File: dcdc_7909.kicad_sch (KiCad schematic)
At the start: 50 parts, among them J1 V_IN, J2 G_IN, J3 RFShield_OnePiece, J4 +10V, J5 G_OUT, J6 -10V, U1 LM2940-SOT223, U2 LT3471, U3 LT3045xMSE, U4 LT3094xMSE

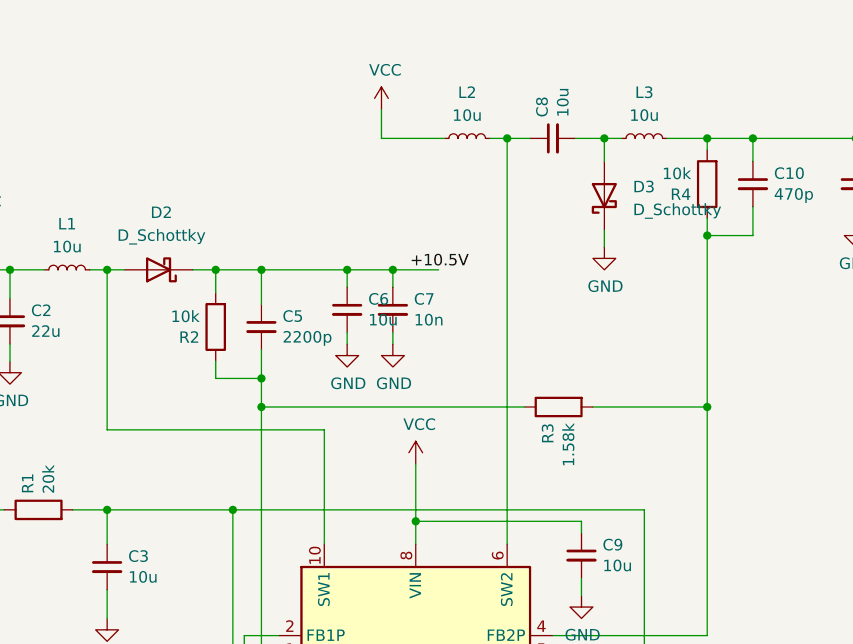
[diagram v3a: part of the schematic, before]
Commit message: Updated BOM.
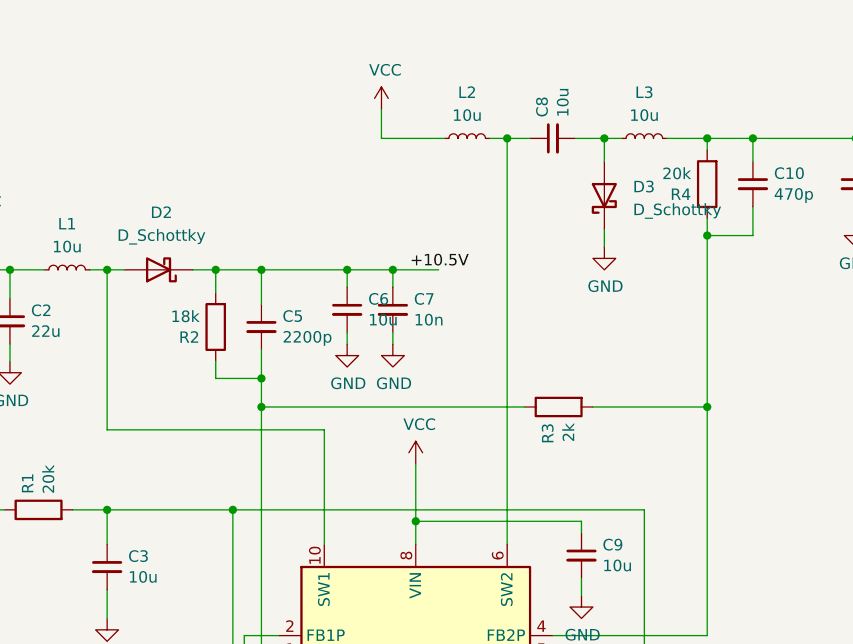
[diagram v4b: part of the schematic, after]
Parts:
- D1: LCSC (none) -> DO NOT POPULATE
- R2: value 10k -> 18k; LCSC (none) -> C25810
- R3: value 1.58k -> 2k; LCSC (none) -> C22975
- R4: value 10k -> 20k; LCSC (none) -> C4184
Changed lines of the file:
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@@
       (effects (font (size 1.27 1.27)) (justify left))
     )
-    (property "Value" "1.58k" (id 1) (at 109.728 114.173 0)
+    (property "Value" "2k" (id 1) (at 109.728 114.173 0)
       (effects (font (size 1.27 1.27)) (justify left))
     )
@@
     )
     (property "Datasheet" "~" (id 3) (at 108.585 112.395 0)
+      (effects (font (size 1.27 1.27)) hide)
+    )
+    (property "LCSC" "C22975" (id 4) (at 108.585 112.395 0)
       (effects (font (size 1.27 1.27)) hide)
     )
@@
   (symbol (lib_id "power:GND") (at 113.665 94.615 0) (unit 1)
     (in_bom yes) (on_board yes)
-    (property "Reference" "#PWR?" (id 0) (at 113.665 100.965 0)
+    (property "Reference" "#PWR0101" (id 0) (at 113.665 100.965 0)
       (effects (font (size 1.27 1.27)) hide)
     )
@@
       (effects (font (size 1.27 1.27)) (justify left))
     )
-    (property "Value" "10k" (id 1) (at 123.317 86.487 0)
+    (property "Value" "20k" (id 1) (at 123.317 86.487 0)
       (effects (font (size 1.27 1.27)) (justify left))
     )
@@
     )
     (property "Datasheet" "~" (id 3) (at 125.095 87.63 0)
+      (effects (font (size 1.27 1.27)) hide)
+    )
+    (property "LCSC" "C4184" (id 4) (at 125.095 87.63 0)
       (effects (font (size 1.27 1.27)) hide)
     )
@@
       (effects (font (size 1.27 1.27)) (justify left))
     )
-    (property "Value" "10k" (id 1) (at 68.707 102.362 0)
+    (property "Value" "18k" (id 1) (at 68.707 102.362 0)
       (effects (font (size 1.27 1.27)) (justify left))
     )
@@
     )
     (property "Datasheet" "~" (id 3) (at 70.485 103.505 0)
+      (effects (font (size 1.27 1.27)) hide)
+    )
+    (property "LCSC" "C25810" (id 4) (at 70.485 103.505 0)
       (effects (font (size 1.27 1.27)) hide)
     )
@@
       (effects (font (size 1.27 1.27)) hide)
     )
+    (property "LCSC" "DO NOT POPULATE" (id 4) (at 45.085 40.005 0)
+      (effects (font (size 1.27 1.27)) hide)
+    )
     (pin "1")
     (pin "2")
@@
     )
     (path "/238e584d-5d8d-4459-9620-7e15c60342c4"
-      (reference "#PWR?") (unit 1) (value "GND") (footprint "")
+      (reference "#PWR0101") (unit 1) (value "GND") (footprint "")
     )
     (path "/aa882a6c-bc17-4b7e-9561-d17811dd5eb5"
@@
     )
     (path "/90e51816-a1d4-45a7-942c-682d8cce5b3b"
-      (reference "R2") (unit 1) (value "10k") (footprint "Resistor_SMD:R_0603_1608Metric")
+      (reference "R2") (unit 1) (value "18k") (footprint "Resistor_SMD:R_0603_1608Metric")
     )
     (path "/18aa7285-da5c-42b6-a485-257c708a9352"
-      (reference "R3") (unit 1) (value "1.58k") (footprint "Resistor_SMD:R_0603_1608Metric")
+      (reference "R3") (unit 1) (value "2k") (footprint "Resistor_SMD:R_0603_1608Metric")
     )
     (path "/3090092e-4c9a-4661-95c3-730de5416b81"
-      (reference "R4") (unit 1) (value "10k") (footprint "Resistor_SMD:R_0603_1608Metric")
+      (reference "R4") (unit 1) (value "20k") (footprint "Resistor_SMD:R_0603_1608Metric")
     )
     (path "/00000000-0000-0000-0000-00005ea01b91"

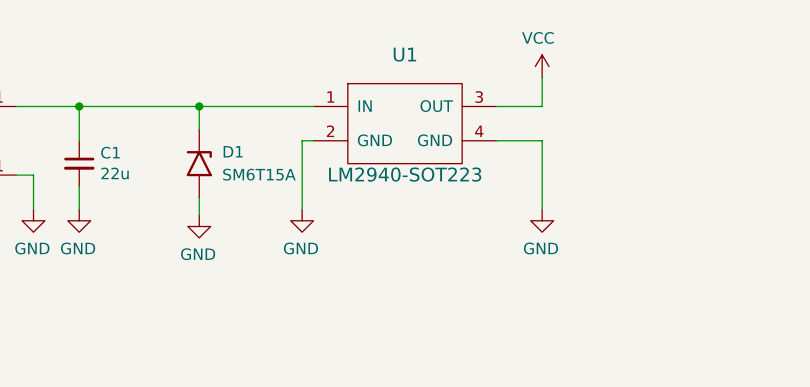
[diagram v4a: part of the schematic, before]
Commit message: Corrected the ground plane.
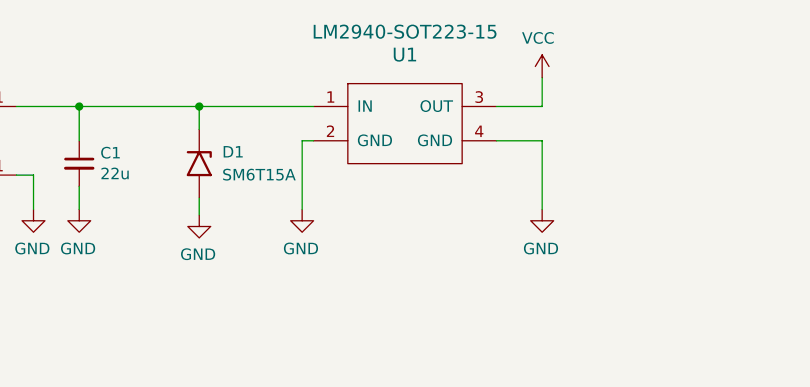
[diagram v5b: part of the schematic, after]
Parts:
- D1: LCSC DO NOT POPULATE -> C80394
- U1: value LM2940-SOT223 -> LM2940-SOT223-15
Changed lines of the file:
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@@
       (effects (font (size 1.524 1.524)))
     )
-    (property "Value" "LM2940-SOT223" (id 1) (at 67.945 41.275 0)
+    (property "Value" "LM2940-SOT223-15" (id 1) (at 67.945 25.4 0)
       (effects (font (size 1.524 1.524)))
     )
@@
       (effects (font (size 1.27 1.27)) hide)
     )
-    (property "LCSC" "DO NOT POPULATE" (id 4) (at 45.085 40.005 0)
+    (property "LCSC" "C80394" (id 4) (at 45.085 40.005 0)
       (effects (font (size 1.27 1.27)) hide)
     )
@@
     )
     (path "/412358be-81ab-4843-8889-7033ea63164a"
-      (reference "U1") (unit 1) (value "LM2940-SOT223") (footprint "Package_TO_SOT_SMD:SOT-223")
+      (reference "U1") (unit 1) (value "LM2940-SOT223-15") (footprint "Package_TO_SOT_SMD:SOT-223")
     )
     (path "/c702bc10-a5cf-47e6-8b8a-b42baf31c984"

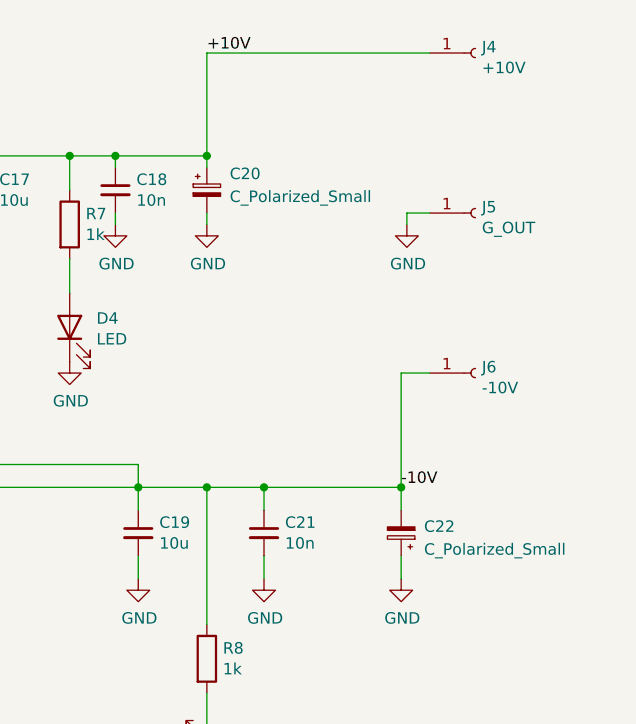
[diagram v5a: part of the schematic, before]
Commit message: New version ready for JLCPCB.
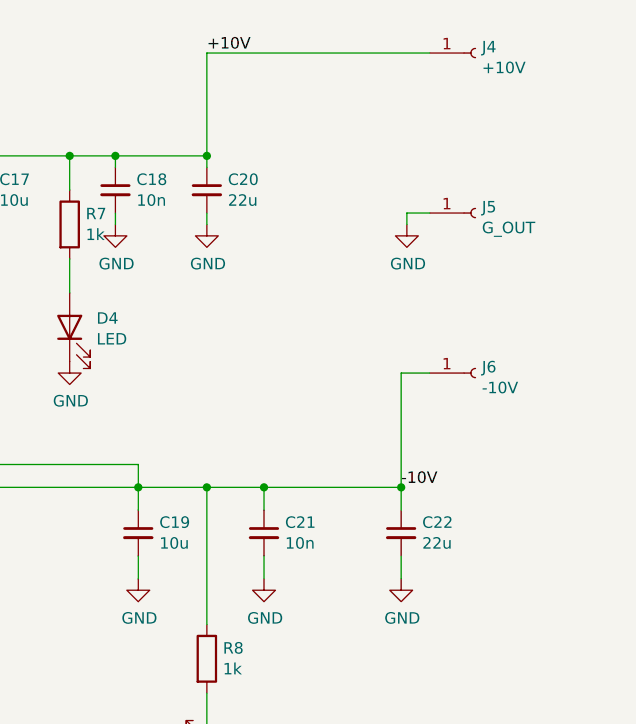
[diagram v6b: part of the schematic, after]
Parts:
- removed C20, C22: C_Polarized_Small, Capacitor_Tantalum_SMD:CP_EIA-3528-21_Kemet-B_Pad1.50x2.35mm_HandSolder, symbol Device:C_Polarized_Small
- added C20, C22: 22u, Capacitor_SMD:C_1206_3216Metric, symbol Device:C_Small
- U3: LCSC DO NOT POPULATE -> C666577
- U4: LCSC DO NOT POPULATE -> C498217
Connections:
- net +10V: now also C20.1
- net -10V: now also C22.1
- net GND: now also C20.2, C22.2

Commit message: Files send for production.
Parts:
- D1: value SM6T15A -> P6SMB20A; LCSC C80394 -> C719321
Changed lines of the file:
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@@
       (effects (font (size 1.27 1.27)) (justify left))
     )
-    (property "Value" "SM6T15A" (id 1) (at 47.625 41.2749 90)
+    (property "Value" "P6SMB20A" (id 1) (at 47.625 41.2749 90)
       (effects (font (size 1.27 1.27)) (justify left))
     )
@@
       (effects (font (size 1.27 1.27)) hide)
     )
-    (property "LCSC" "C80394" (id 4) (at 45.085 40.005 0)
+    (property "LCSC" "C719321" (id 4) (at 45.085 40.005 0)
       (effects (font (size 1.27 1.27)) hide)
     )
@@
     )
     (path "/f11161ac-374d-4d0b-9af2-4499fab11bbf"
-      (reference "D1") (unit 1) (value "SM6T15A") (footprint "Diode_SMD:D_SMB")
+      (reference "D1") (unit 1) (value "P6SMB20A") (footprint "Diode_SMD:D_SMB")
     )
     (path "/368e7021-7891-43f1-98f4-75d38a18a3eb"

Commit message: WIP on version 2.1, routing mostly done.
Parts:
- removed J3: RFShield_OnePiece, RF_Shielding:Laird_Technologies_BMI-S-102_16.50x16.50mm, symbol Device:RFShield_OnePiece
- added C3: 4u7, Capacitor_SMD:C_1206_3216Metric, symbol Device:C_Small
- added C8: 22u, Capacitor_SMD:C_1210_3225Metric, symbol Device:C_Small
- added J3, J4, J5, J6: RFShield_Clip, marcin_library:S0971-46R, symbol marcin_library:RFShield_Clip
- added L2: 10u, Inductor_SMD:L_Vishay_IHLP-1616, symbol Device:L_Small
- added NT1, NT2: NetTie_2, NetTie:NetTie-2_SMD_Pad0.5mm, symbol Device:NetTie_2
- added R2, R4: DNP, Resistor_SMD:R_0402_1005Metric, symbol Device:R
- C1: renamed from C2; footprint Capacitor_SMD:C_0805_2012Metric_Pad1.18x1.45mm_HandSolder -> Capacitor_SMD:C_1210_3225Metric; LCSC C45783 -> C426653; PN (none) -> Murata GCM32EC71E226KE36
- C10: renamed from C8; value 10u -> 4u7; footprint Capacitor_SMD:C_0603_1608Metric -> Capacitor_SMD:C_1206_3216Metric; LCSC C96446 -> C29823
- C11: renamed from C9; value 10u -> 22u; footprint Capacitor_SMD:C_0603_1608Metric -> Capacitor_SMD:C_1210_3225Metric; LCSC C96446 -> C426653; PN (none) -> Murata GCM32EC71E226KE36
- C12: renamed from C10; footprint Capacitor_SMD:C_0603_1608Metric -> Capacitor_SMD:C_0402_1005Metric
- C13: renamed from C11; value 10u -> 22u; footprint Capacitor_SMD:C_0603_1608Metric -> Capacitor_SMD:C_1210_3225Metric; LCSC C96446 -> C426653; PN (none) -> Murata GCM32EC71E226KE36
- C14: renamed from C12; footprint Capacitor_SMD:C_0603_1608Metric -> Capacitor_SMD:C_0402_1005Metric
- C15: renamed from C13; value 10u -> 22u; footprint Capacitor_SMD:C_0805_2012Metric_Pad1.18x1.45mm_HandSolder -> Capacitor_SMD:C_1210_3225Metric; LCSC C15850 -> C426653; PN (none) -> Murata GCM32EC71E226KE36
- C16: renamed from C14; value 10u -> 22u; footprint Capacitor_SMD:C_0805_2012Metric_Pad1.18x1.45mm_HandSolder -> Capacitor_SMD:C_1210_3225Metric; LCSC C15850 -> C426653; PN (none) -> Murata GCM32EC71E226KE36
- C17: renamed from C15; footprint Capacitor_SMD:C_0805_2012Metric_Pad1.18x1.45mm_HandSolder -> Capacitor_SMD:C_0805_2012Metric
- C18: renamed from C16; footprint Capacitor_SMD:C_0805_2012Metric_Pad1.18x1.45mm_HandSolder -> Capacitor_SMD:C_0805_2012Metric
- C19: renamed from C17; value 10u -> 22u; footprint Capacitor_SMD:C_0805_2012Metric_Pad1.18x1.45mm_HandSolder -> Capacitor_SMD:C_1210_3225Metric; LCSC C15850 -> C426653; PN (none) -> Murata GCM32EC71E226KE36
- C2: renamed from C1; footprint Capacitor_SMD:C_0805_2012Metric_Pad1.18x1.45mm_HandSolder -> Capacitor_SMD:C_1210_3225Metric; LCSC C45783 -> C426653; PN (none) -> Murata GCM32EC71E226KE36
- C20: renamed from C19; value 10u -> 22u; footprint Capacitor_SMD:C_0805_2012Metric_Pad1.18x1.45mm_HandSolder -> Capacitor_SMD:C_1210_3225Metric; LCSC C15850 -> C426653; PN (none) -> Murata GCM32EC71E226KE36
- C21: renamed from C18; footprint Capacitor_SMD:C_0603_1608Metric -> Capacitor_SMD:C_0402_1005Metric
- C22: renamed from C20; footprint Capacitor_SMD:C_1206_3216Metric -> Capacitor_SMD:C_1210_3225Metric; LCSC C12891 -> C426653; PN (none) -> Murata GCM32EC71E226KE36
- C23: renamed from C21; footprint Capacitor_SMD:C_0603_1608Metric -> Capacitor_SMD:C_0402_1005Metric
- C24: renamed from C22; footprint Capacitor_SMD:C_1206_3216Metric -> Capacitor_SMD:C_1210_3225Metric; LCSC C12891 -> C426653; PN (none) -> Murata GCM32EC71E226KE36
- C5: renamed from C4; footprint Capacitor_SMD:C_0603_1608Metric -> Capacitor_SMD:C_0402_1005Metric
- C6: renamed from C5; footprint Capacitor_SMD:C_0603_1608Metric -> Capacitor_SMD:C_0402_1005Metric
- C7: renamed from C6; value 10u -> 22u; footprint Capacitor_SMD:C_0603_1608Metric -> Capacitor_SMD:C_1210_3225Metric; LCSC C96446 -> C426653; PN (none) -> Murata GCM32EC71E226KE36
- C9: renamed from C7; footprint Capacitor_SMD:C_0603_1608Metric -> Capacitor_SMD:C_0402_1005Metric
- J1, J2: footprint Connector_Wire:SolderWirePad_1x01_Drill1.2mm -> Connector_Wire:SolderWire-0.75sqmm_1x01_D1.25mm_OD3.5mm
- J7: renamed from J4; footprint Connector_Wire:SolderWirePad_1x01_Drill1.2mm -> Connector_Wire:SolderWire-0.75sqmm_1x01_D1.25mm_OD3.5mm
- J8: renamed from J5; footprint Connector_Wire:SolderWirePad_1x01_Drill1.2mm -> Connector_Wire:SolderWire-0.75sqmm_1x01_D1.25mm_OD3.5mm
- J9: renamed from J6; footprint Connector_Wire:SolderWirePad_1x01_Drill1.2mm -> Connector_Wire:SolderWire-0.75sqmm_1x01_D1.25mm_OD3.5mm
- R1: footprint Resistor_SMD:R_0603_1608Metric -> Resistor_SMD:R_0402_1005Metric
- R3: renamed from R2; footprint Resistor_SMD:R_0603_1608Metric -> Resistor_SMD:R_0402_1005Metric
- R5: renamed from R3; footprint Resistor_SMD:R_0603_1608Metric -> Resistor_SMD:R_0402_1005Metric
- R6: renamed from R4; footprint Resistor_SMD:R_0603_1608Metric -> Resistor_SMD:R_0402_1005Metric
- TP1, TP2: footprint TestPoint:TestPoint_Pad_D2.0mm -> TestPoint:TestPoint_THTPad_D1.0mm_Drill0.5mm
- renumbered C3 to C4, L2 to L3, L3 to L4, R8 to R10, R5 to R7, R6 to R8, R7 to R9
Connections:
- net +10V: now also NT1.2; no longer U3.10 (OUTS)
- net -10V: now also NT2.2; no longer U4.10 (OUTS)
- net GND: now also C8.2, J3.1 (Shield), J4.1 (Shield), J5.1 (Shield), J6.1 (Shield), L2.1, R2.1
- net VCC: now also C8.1
- net at C5.1, U2.2 (FB1P), U2.3 (VREF): now also R4.1
- net at C6.2, R3.1, R5.1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: now also R2.2
- net at C12.2, R5.2, R6.1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: now also R4.2
- net at L1.2, U2.10 (SW1): now also C3.1; no longer D2.2 (A)
- new net: NT1.1, U3.10 (OUTS)
- new net: NT2.1, U4.10 (OUTS)
- new net: C3.2, D2.2 (A), L2.2
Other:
- moved on the sheet: C1, C19, C21, C22, C6, C7, C9, D2, D4, L1, R3, R9
